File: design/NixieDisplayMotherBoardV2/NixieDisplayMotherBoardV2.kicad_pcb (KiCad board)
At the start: 2 copper layers, 110.5 x 66 mm, 83 parts, among them J1 Data Connector, J2 High Voltage Connector, J3 Barrel_Jack, J4 SWD, Q1 PMBT3904, Q2 PMV50EPEAR, Q3 IRF840A, SW1 SW_SPDT, SW2 Prev BTN, SW3 Select BTN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

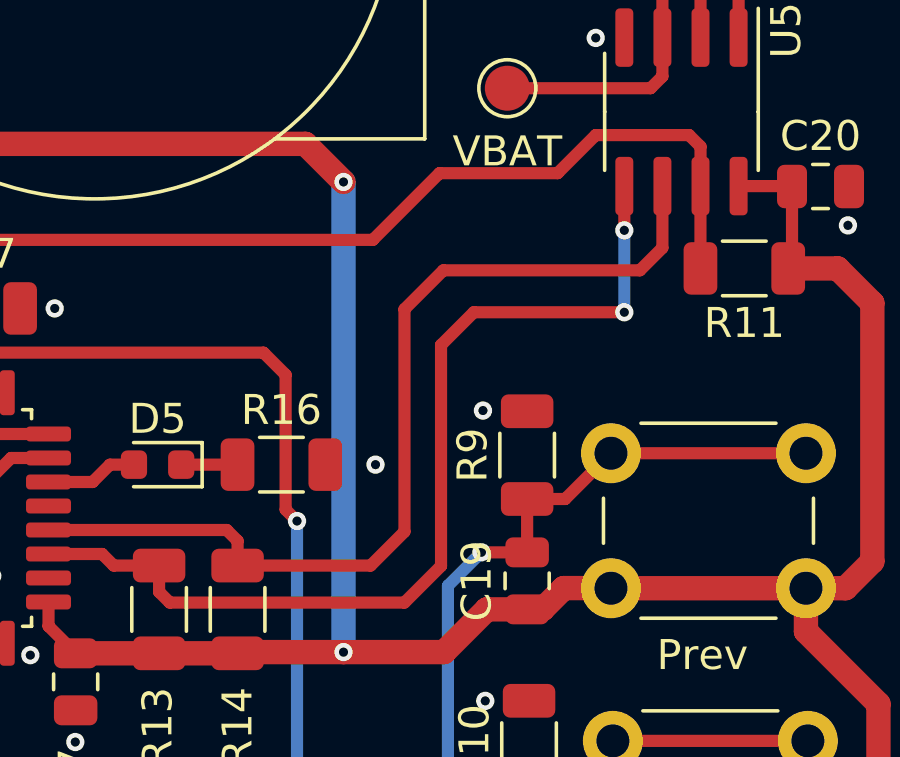
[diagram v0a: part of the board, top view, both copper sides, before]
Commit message: Fixing I2C connection on the design
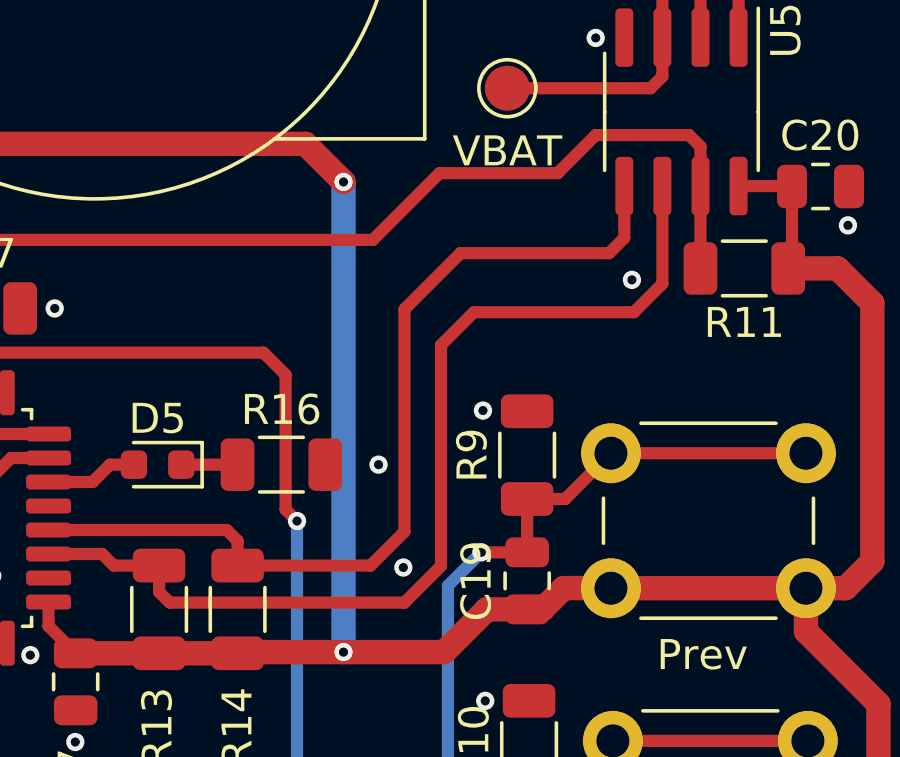
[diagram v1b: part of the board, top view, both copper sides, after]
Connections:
- U5 pad 5: /uController/I2C1_SCL -> /uController/I2C1_SDA
- U5 pad 6: /uController/I2C1_SDA -> /uController/I2C1_SCL
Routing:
- net /uController/I2C1_SDA: track 32.2 -> 30.8 mm
- net /uController/I2C1_SCL: track 32.9 -> 33.6 mm, vias 2 -> 0
- net /GND: vias 63 -> 65
